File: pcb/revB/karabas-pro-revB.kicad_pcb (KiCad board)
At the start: 2 copper layers, 101.6 x 147.3 mm, 138 parts, among them CON1 CF-CARD, CON2 SD, CON3 VGA, CON4 Joystick, CON5 Keyboard, CON6 Mouse, CON7 Audio, CON8 5V DC, J1 Floppy, J2 FPGA JTAG, J3 Floppy 5V, J4 uBus, J5 AVR JTAG, J6 AVR UART, SW1 SW_Push, SW2 SW_Push, U1 EP4CE6E22C8N, U10 ESP-12E, U11 TDA1543, U12 AMS1117-3.3, U13 AMS1117-2.5, U14 AMS1117-1.2, U17 74LS06, U18 74LS38, U2 CY62167EV30, U3 M25P16, U4 EPM3128ATC100-5, U5 ATMEGA328-AU, U6 MB8877A, U7 TXB0104PW, U8 TXB0104PW, U9 DS1307Z+, X1 SG-7050CAN, Y1 32768Hz, Y2 16MHz

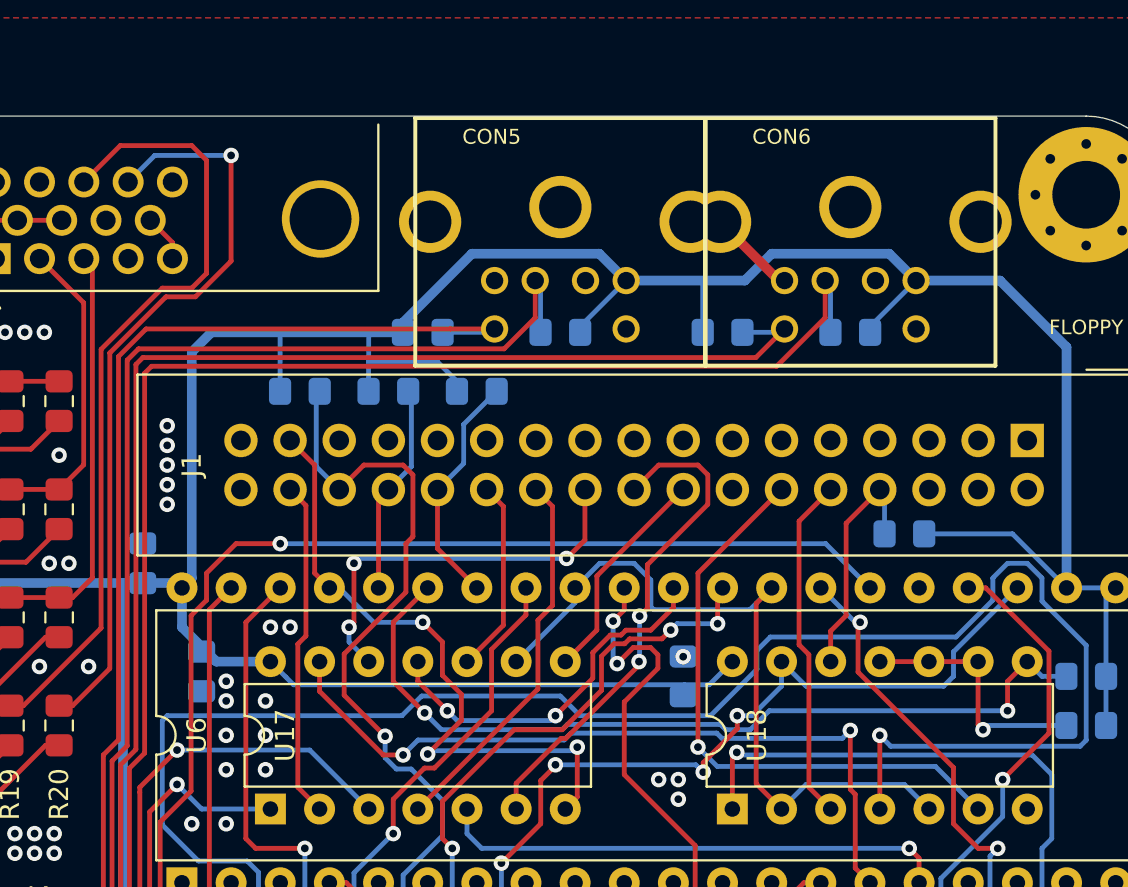
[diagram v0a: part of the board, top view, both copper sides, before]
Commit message: Updated PS/2 footprint
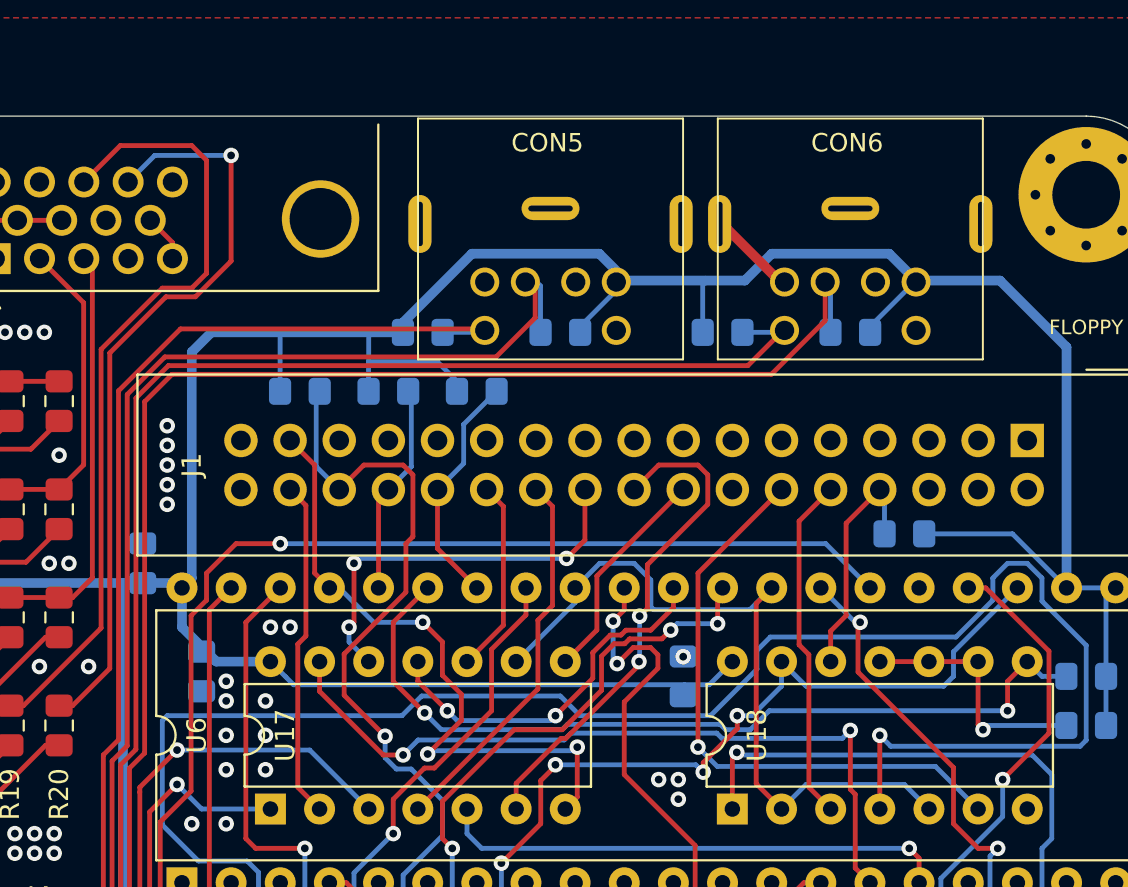
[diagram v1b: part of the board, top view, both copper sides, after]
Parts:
- CON5, CON6: footprint footprints:MDIN06SS -> footprints:MINI_DIN_6_33PRIMARY
- moved CON5 6.37 mm to (168.9, 31.8), turned to 0 degrees
- moved CON6 6.35 mm to (184.4, 31.8), turned to 0 degrees
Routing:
- net /PS2_KB_DATA: track 161.5 -> 160.5 mm
- net /PS2_KB_CLK: track 159.5 -> 158.5 mm
- net /PS2_MS_CLK: track 172.3 -> 171.3 mm
- net /PS2_MS_DATA: track 172.9 -> 172.1 mm
